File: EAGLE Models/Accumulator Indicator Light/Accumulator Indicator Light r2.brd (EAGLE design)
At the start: 39.4 x 48.9 mm, 9 parts, among them U1 LR8DPACK

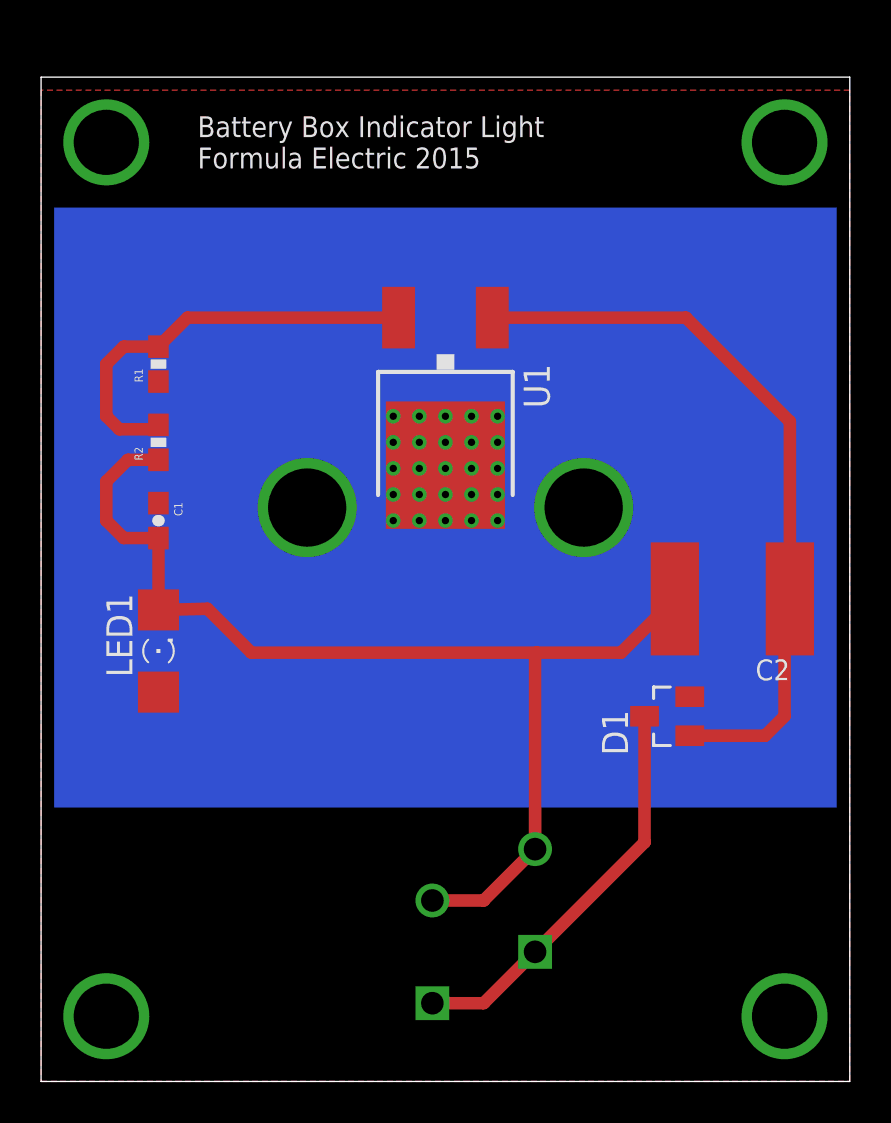
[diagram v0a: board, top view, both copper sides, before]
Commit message: Fixed problem with AIL
Zener was too small and board was not fused
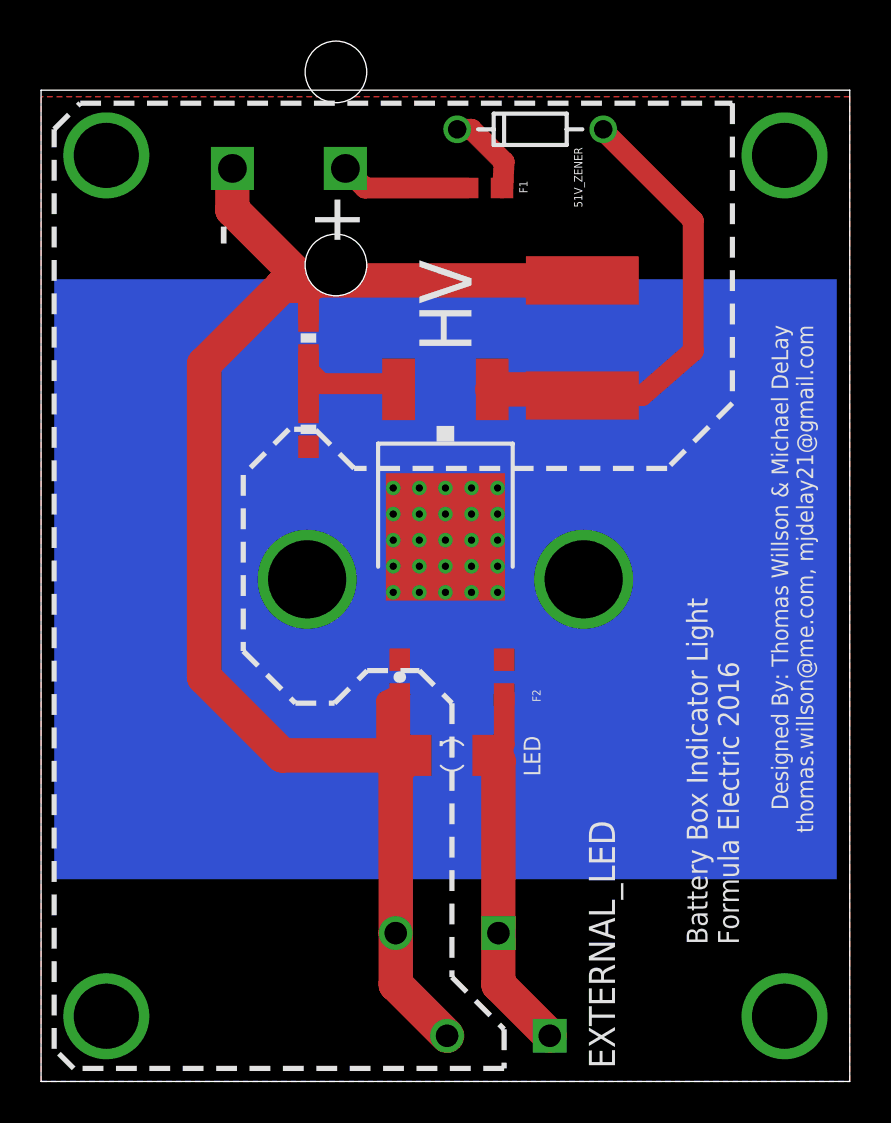
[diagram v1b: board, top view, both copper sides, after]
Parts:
- removed D1: 51V, diode:SOT23
- removed LED1: (no value), led:1206
- added 51V_ZENER: 1N5942BRLGOSCT-ND, SparkFun-DiscreteSemi:DIODE-ZENER
- added EXTERNAL_LED: CONN_2, formula electric:CONNECTOR_2
- added F1, F2: PTC0603, SparkFun-PowerIC:0603
- added LED: (no value), led:1206
- HV: value CONN_2 -> 5566-2; device formula electric:CONNECTOR_2 -> con-molex:5566-2
- moved HV 41.2 mm to (12.1, 44.5)
- moved C2 14.6 mm to (26.4, 36.2), turned to 90 degrees
- moved C1 14.0 mm to (17.5, 19.7)
- moved R2 8.90 mm to (13.0, 36.2), turned to 270 degrees
- moved R1 7.96 mm to (13.0, 31.8)
- moved U$1 3.49 mm to (19.7, 24.4)
- moved U1 3.49 mm to (19.7, 28.9)
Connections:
- new net N$10: EXTERNAL_LED.1, EXTERNAL_LED.2, F2.2, LED.A
- new net N$8: 51V_ZENER.P$1, F1.2
- net HV+: now also F1.1; no longer D1.3, HV.1
- net HV-: now also EXTERNAL_LED.3, EXTERNAL_LED.4, HV.1, LED.C; no longer HV.3, HV.4, LED1.C
- net N$: now also 51V_ZENER.P$2; no longer D1.1
- net N$2: now also F2.1; no longer LED1.A
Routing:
- net HV-: track 54.0 -> 77.3 mm
- net N$10: track 0.00 -> 18.0 mm
- net HV+: track 19.7 -> 6.32 mm
- net N$1: track 20.6 -> 8.25 mm
- net N$: track 36.0 -> 24.7 mm
- net N$8: track 0.00 -> 4.23 mm
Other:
- board size 39.4 x 48.9 mm -> 39.4 x 48.3 mm
- board text added: "Battery Box Indicator Light Formula Electric 2016"
- board text added: "Designed By: Thomas Willson & Michael DeLay thomas.willson@me.com, mjdelay21@gmail.com"
- board text removed: "Battery Box Indicator Light Formula Electric 2015"
- board text removed: "Designed By: Thomas Willson thomas.willson@me.com"
